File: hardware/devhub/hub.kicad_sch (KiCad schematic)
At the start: 34 parts, among them J2 USB-C UPSTREAM, J3 PORTA 7 (scorta), U2 USB2517I-JZX, Y1 24MHz

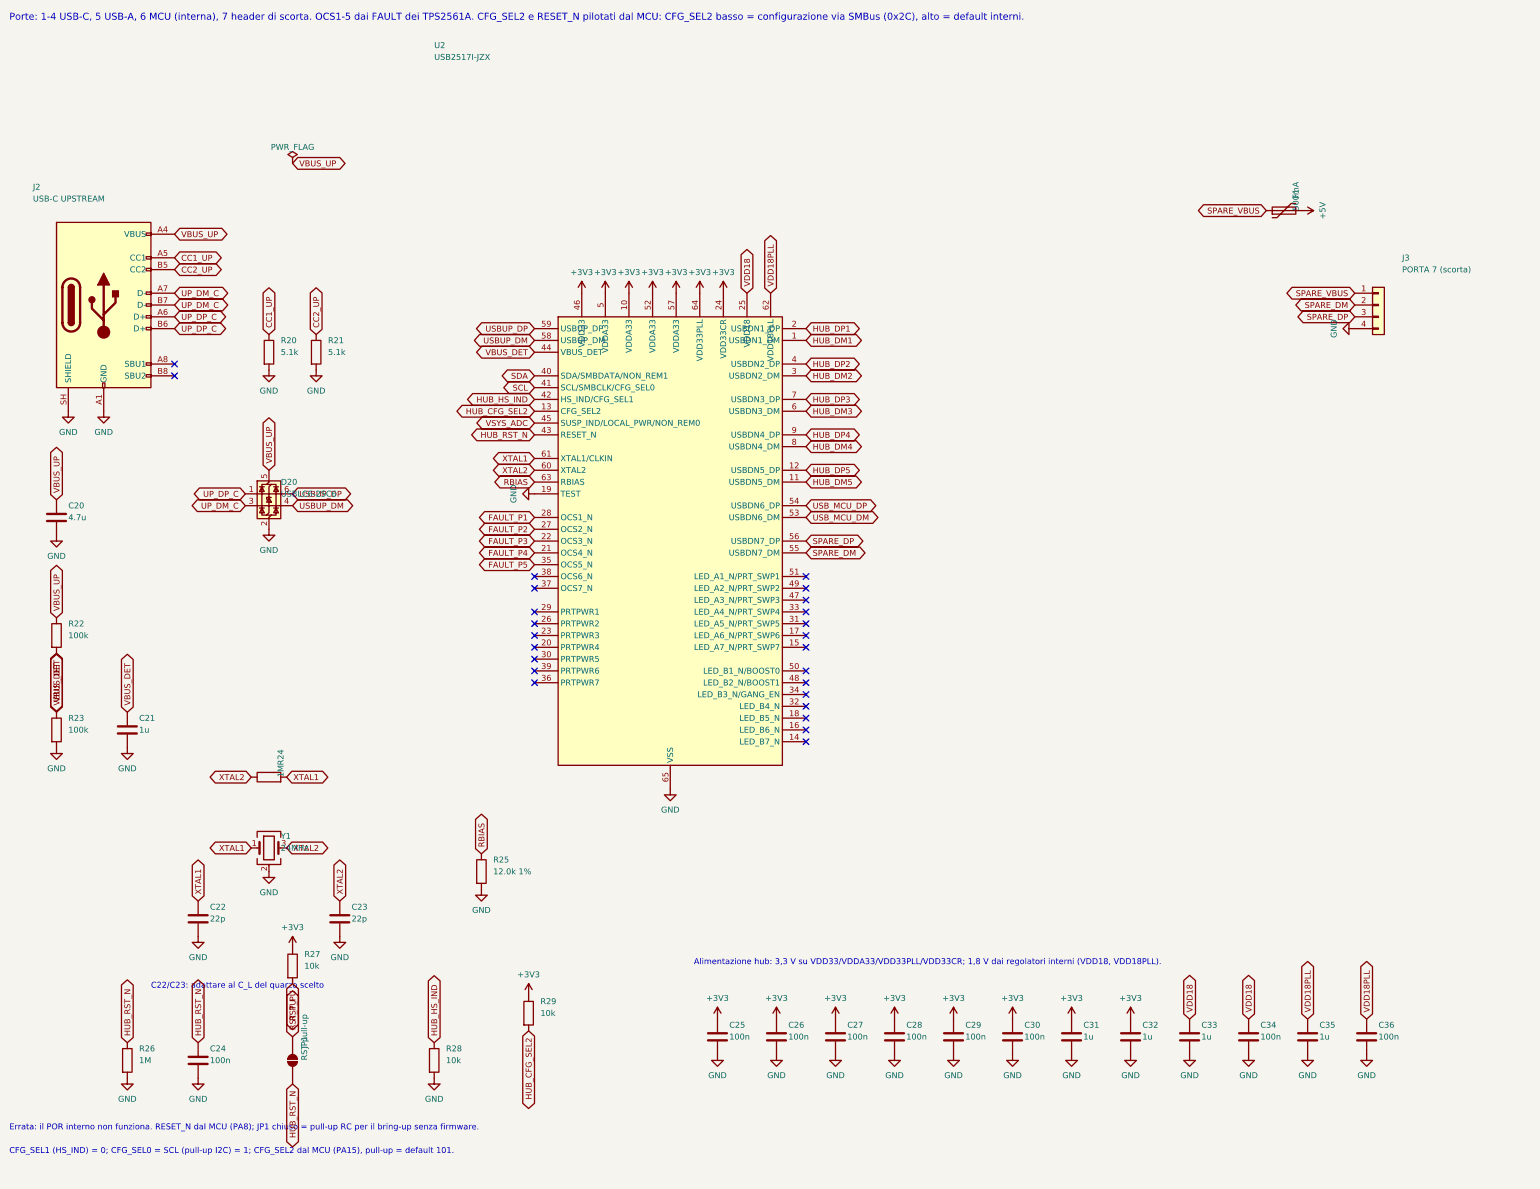
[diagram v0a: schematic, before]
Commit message: Schematic v0.2: hub reset supervisor, 1 A LDO, reorganized sheets, USB connectors and crystal
Functional changes:
- USB2517 RESET_N with pull-up and MCP120T-300 supervisor, wired-OR with
  the MCU (open-drain): resetting the MCU no longer resets the hub, so the
  ST DFU bootloader is reachable through it (D16/D17).
- 3.3 V LDO: AP7361C-33E (1 A, SOT-223) instead of AP2112K, which
  dissipated too much with the hub load.
- 74HC595 /OE on PB6 with pull-up: LEDs off until firmware enables them.
- Orange D93 instead of blue, USB-A bulk capacitance >= 120 uF, relay coil
  pinout fixed, snubbers marked DNP, Cliff FCR7350 banana jack footprints.
- D18: horizontal USB connectors, GCT USB4105-GF-A (USB-C) and Kycon
  KUSBX-AS1N-B (USB-A).
- D19: YXC X322524MOB4SI 24 MHz crystal (C_L 12 pF), 15 pF C0G load caps.

Layout: nearby parts wired directly, every net still explicitly named;
local labels inside sheets, global only across sheets, hierarchical for
ports. Files saved with KiCad 10.

Connectivity checked against the previous netlist, ERC clean.
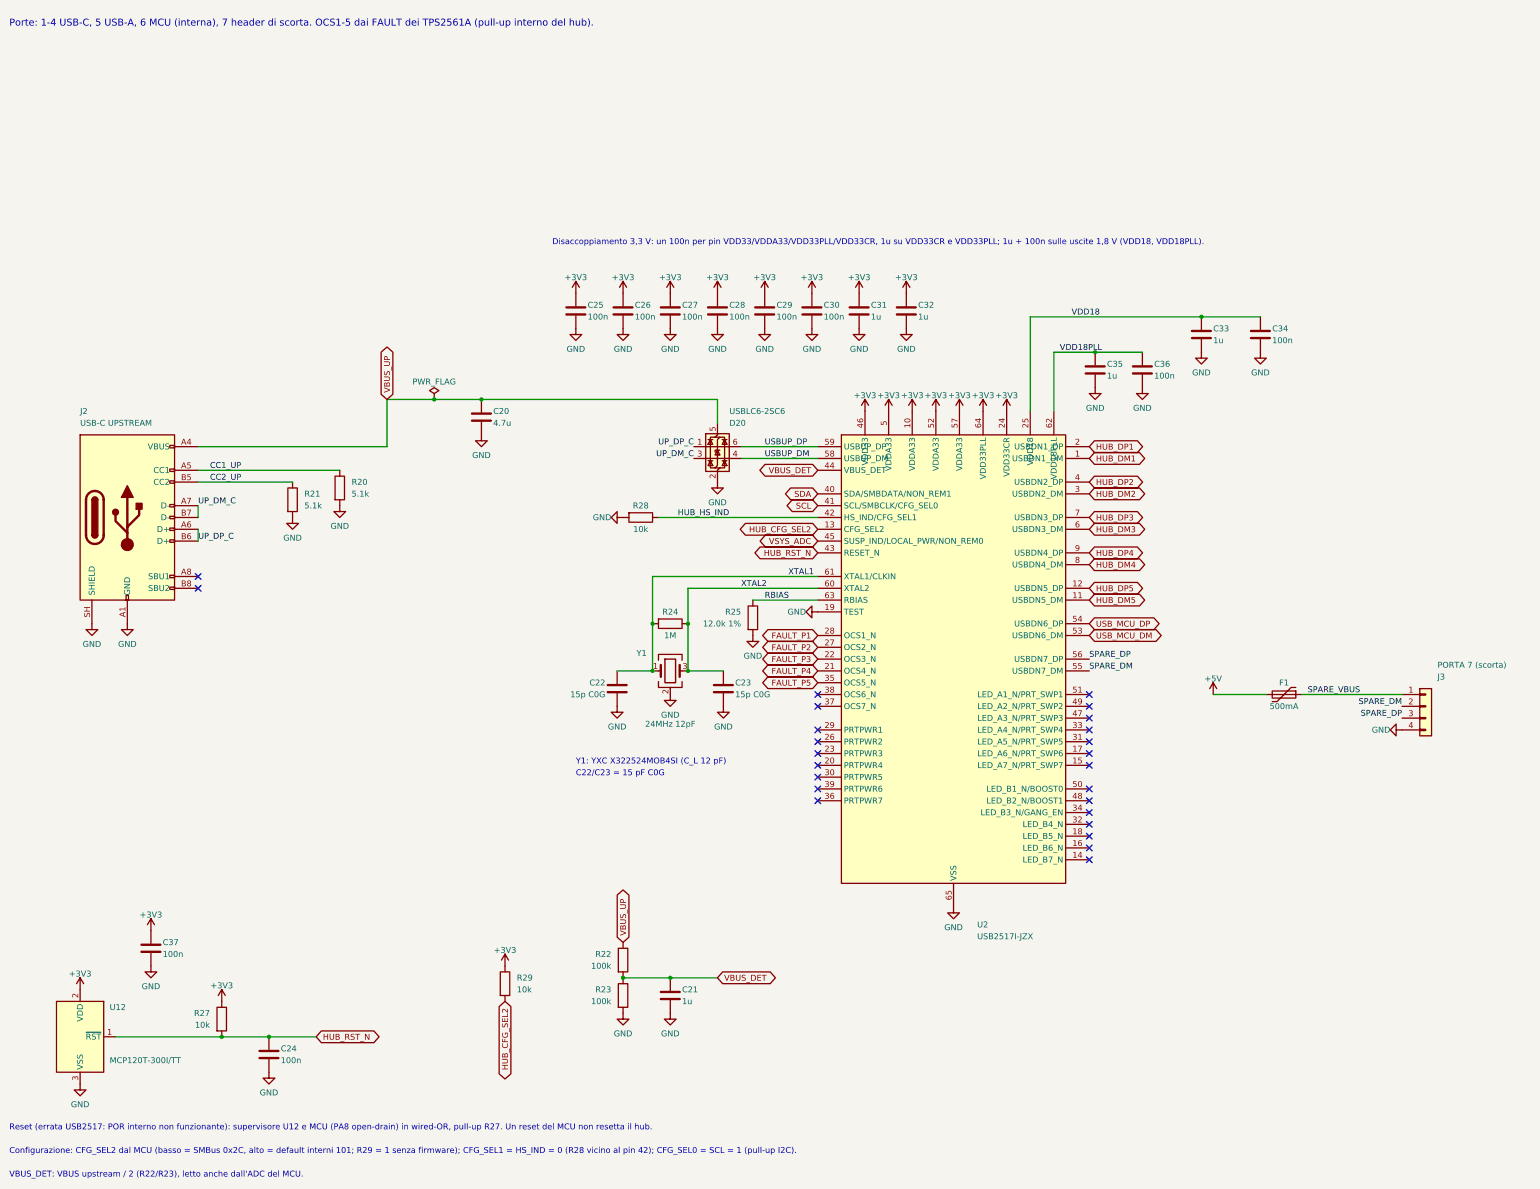
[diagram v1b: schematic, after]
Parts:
- removed JP1: RST pull-up, Jumper:SolderJumper-2_P1.3mm_Open_RoundedPad1.0x1.5mm, symbol Jumper:SolderJumper_2_Open
- removed R26: 1M, Resistor_SMD:R_0603_1608Metric, symbol Device:R
- added C37: 100n, Capacitor_SMD:C_0603_1608Metric, symbol Device:C
- added U12: MCP120T-300I/TT, Package_TO_SOT_SMD:SOT-23, symbol Power_Supervisor:MCP120-xxxxTT
- C22, C23: value 22p -> 15p C0G
- Y1: value 24MHz -> 24MHz 12pF
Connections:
- net RST_PU is gone; now on net HUB_RST_N: R27.2
- net +3V3: now also C37.1, U12.2 (VDD)
- net GND: now also C37.2, U12.3 (VSS)
- net HUB_RST_N: now also U12.1 (~{RST})
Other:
- note added: "C22/C23 = 15 pF C0G"
- note added: "Configurazione: CFG_SEL2 dal MCU (basso = SMBus 0x2C, alto = default interni 101; R29 = 1 senza firmware); CFG_SEL1 = HS_IND = 0 (R28 vicino al pin 42); CFG_SEL0 = SCL = 1 (pull-up I2C)."
- note added: "Disaccoppiamento 3,3 V: un 100n per pin VDD33/VDDA33/VDD33PLL/VDD33CR, 1u su VDD33CR e VDD33PLL; 1u + 100n sulle uscite 1,8 V (VDD18, VDD18PLL)."
- note added: "Porte: 1-4 USB-C, 5 USB-A, 6 MCU (interna), 7 header di scorta. OCS1-5 dai FAULT dei TPS2561A (pull-up interno del hub)."
- note added: "Reset (errata USB2517: POR interno non funzionante): supervisore U12 e MCU (PA8 open-drain) in wired-OR, pull-up R27. Un reset del MCU non resetta il hub."
- note added: "VBUS_DET: VBUS upstream / 2 (R22/R23), letto anche dall'ADC del MCU."
- note added: "Y1: YXC X322524MOB4SI (C_L 12 pF)"
- note removed: "Alimentazione hub: 3,3 V su VDD33/VDDA33/VDD33PLL/VDD33CR; 1,8 V dai regolatori interni (VDD18, VDD18PLL)."
- note removed: "C22/C23: adattare al C_L del quarzo scelto"
- note removed: "CFG_SEL1 (HS_IND) = 0; CFG_SEL0 = SCL (pull-up I2C) = 1; CFG_SEL2 dal MCU (PA15), pull-up = default 101."
- note removed: "Errata: il POR interno non funziona. RESET_N dal MCU (PA8); JP1 chiuso = pull-up RC per il bring-up senza firmware."
- note removed: "Porte: 1-4 USB-C, 5 USB-A, 6 MCU (interna), 7 header di scorta. OCS1-5 dai FAULT dei TPS2561A. CFG_SEL2 e RESET_N pilotati dal MCU: CFG_SEL2 basso = configurazione via SMBus (0x2C), alto = default interni."

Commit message: Review 02, R02-05: drop RF-16, logic powered from the supply only (D32)
Removed D3; VBUS_DET and VSYS_ADC moved to 5 V tolerant pins (PA6, PA7).
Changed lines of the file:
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@@
 		)
 	)
-	(global_label "VBUS_UP"
-		(shape bidirectional)
+	(label "VBUS_UP"
 		(at 91.44 96.52 90)
-		(fields_autoplaced yes)
-		(effects
-			(font
-				(size 1.27 1.27)
-			)
-			(justify left)
-		)
-		(property "Intersheetrefs" "${INTERSHEET_REFS}"
-			(at 91.44 96.52 0)
-			(hide yes)
-			(show_name no)
-			(do_not_autoplace no)
-			(effects
-				(font
-					(size 1.27 1.27)
-				)
-			)
+		(effects
+			(font
+				(size 1.27 1.27)
+			)
+			(justify left bottom)
 		)
 	)
@@
 		)
 	)
-	(global_label "VBUS_UP"
-		(shape bidirectional)
+	(label "VBUS_UP"
 		(at 142.24 213.36 90)
-		(fields_autoplaced yes)
-		(effects
-			(font
-				(size 1.27 1.27)
-			)
-			(justify left)
-		)
-		(property "Intersheetrefs" "${INTERSHEET_REFS}"
-			(at 142.24 213.36 0)
-			(hide yes)
-			(show_name no)
-			(do_not_autoplace no)
-			(effects
-				(font
-					(size 1.27 1.27)
-				)
-			)
-		)
-	)
+		(effects
+			(font
+				(size 1.27 1.27)
+			)
+			(justify left bottom)
+		)
+	)

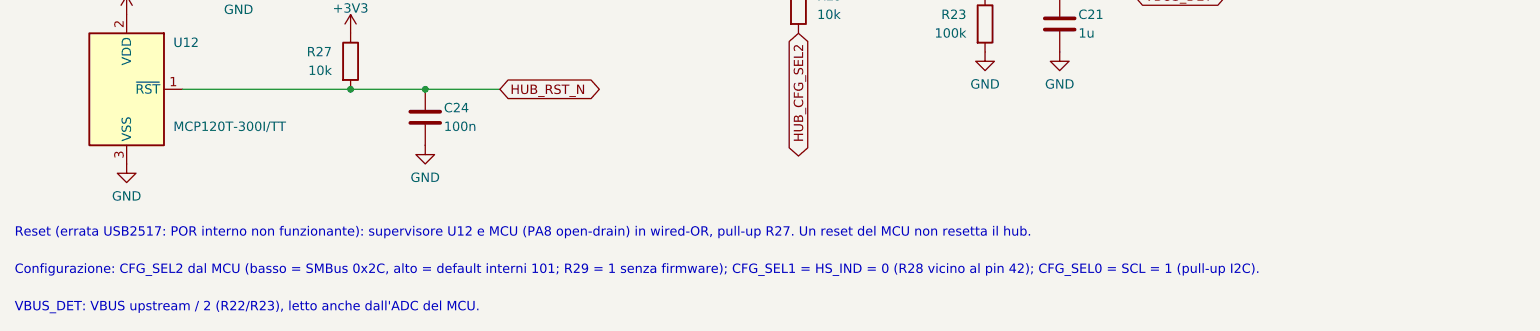
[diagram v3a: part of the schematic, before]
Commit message: Review 02, R02-07: MCU pins compatible with UCPD and the ST bootloader (D34)
Hub reset moved to PF1, pull-downs on the DBCC pins.
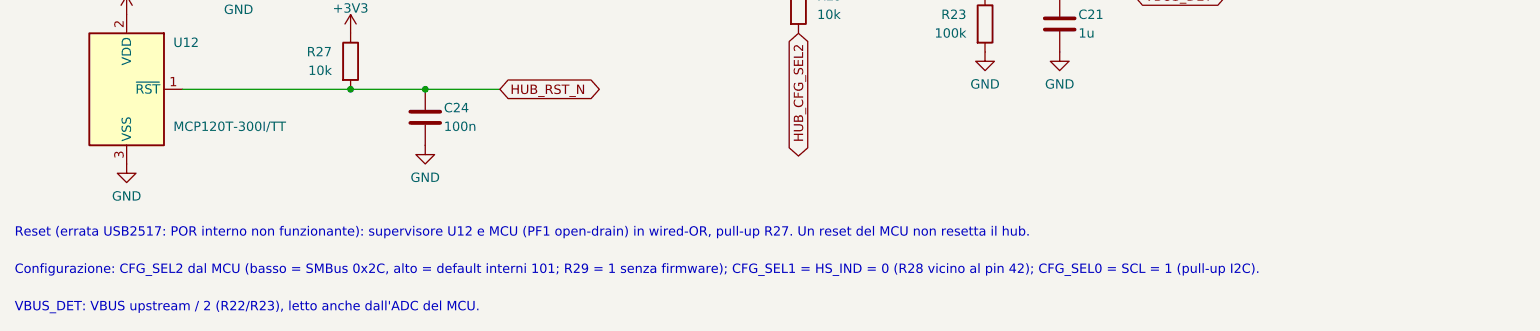
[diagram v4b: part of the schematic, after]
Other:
- note added: "Reset (errata USB2517: POR interno non funzionante): supervisore U12 e MCU (PF1 open-drain) in wired-OR, pull-up R27. Un reset del MCU non resetta il hub."
- note removed: "Reset (errata USB2517: POR interno non funzionante): supervisore U12 e MCU (PA8 open-drain) in wired-OR, pull-up R27. Un reset del MCU non resetta il hub."
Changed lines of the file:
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@@
 		)
 	)
-	(text "Reset (errata USB2517: POR interno non funzionante): supervisore U12 e MCU (PA8 open-drain) in wired-OR, pull-up R27. Un reset del MCU non resetta il hub."
+	(text "Reset (errata USB2517: POR interno non funzionante): supervisore U12 e MCU (PF1 open-drain) in wired-OR, pull-up R27. Un reset del MCU non resetta il hub."
 		(exclude_from_sim no)
 		(at 10.16 254 0)
